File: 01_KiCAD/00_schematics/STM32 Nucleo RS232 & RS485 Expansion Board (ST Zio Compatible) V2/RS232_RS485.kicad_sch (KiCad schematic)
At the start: 28 parts, among them J1 HD-A(Y), J2 HD-B(Z), J3 TERM (A/B), J4 TERM (Y/Z), J5 1190299, J6 CONN D-SUB PLUG 9POS TH, J7 TCVR PWR, U3 THVD4431

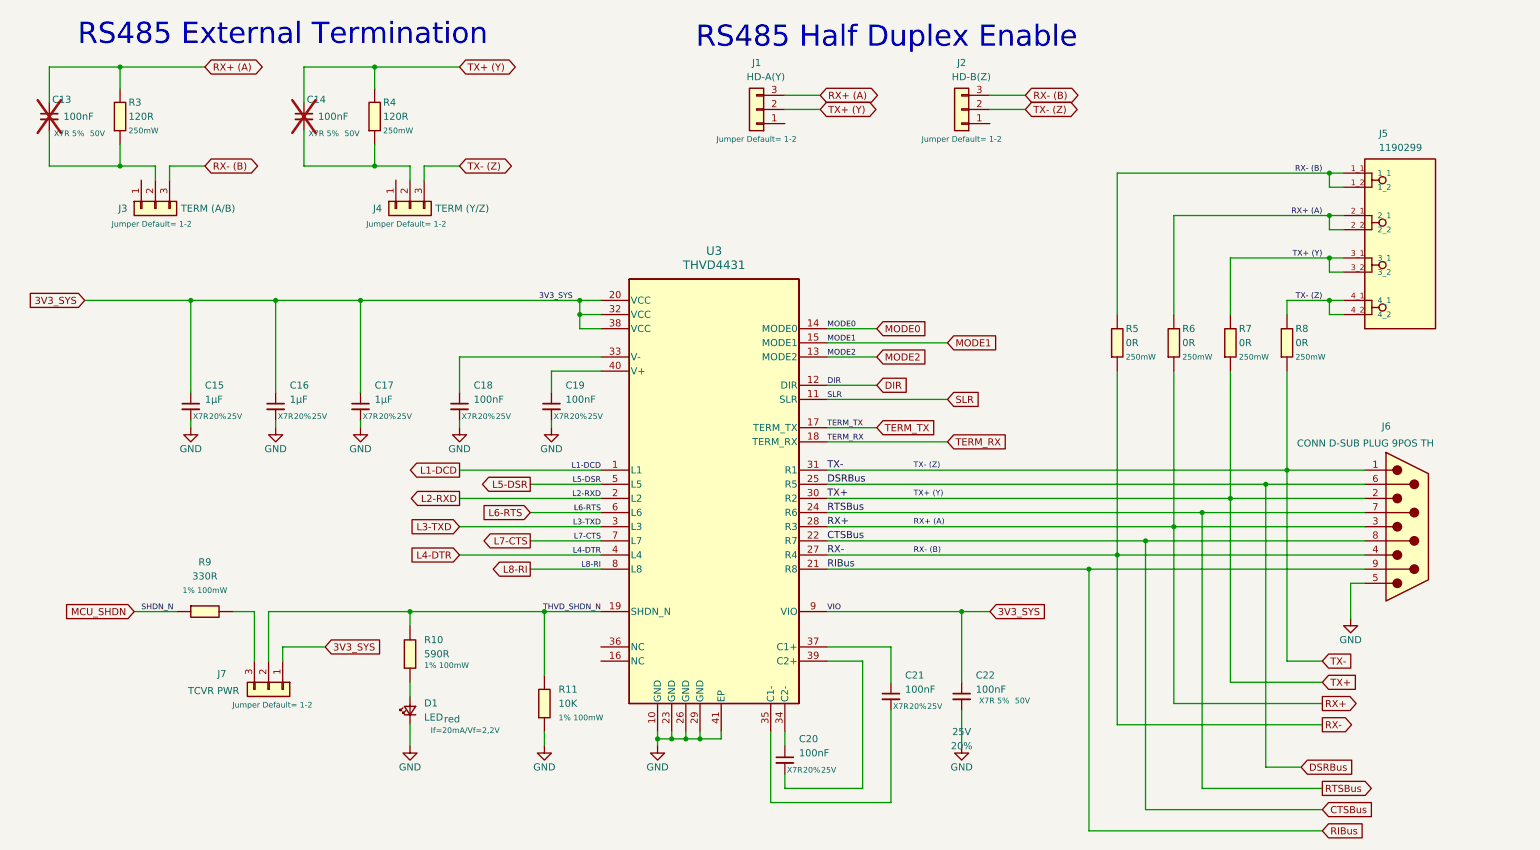
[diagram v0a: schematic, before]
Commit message: Final revision checkup
After BOM-update and corrected some footprints and package sizes for resistors and capacitors, updated the PCB to "HW REV A0.2" as final PCB layout. Need to run DRC check before final approval.
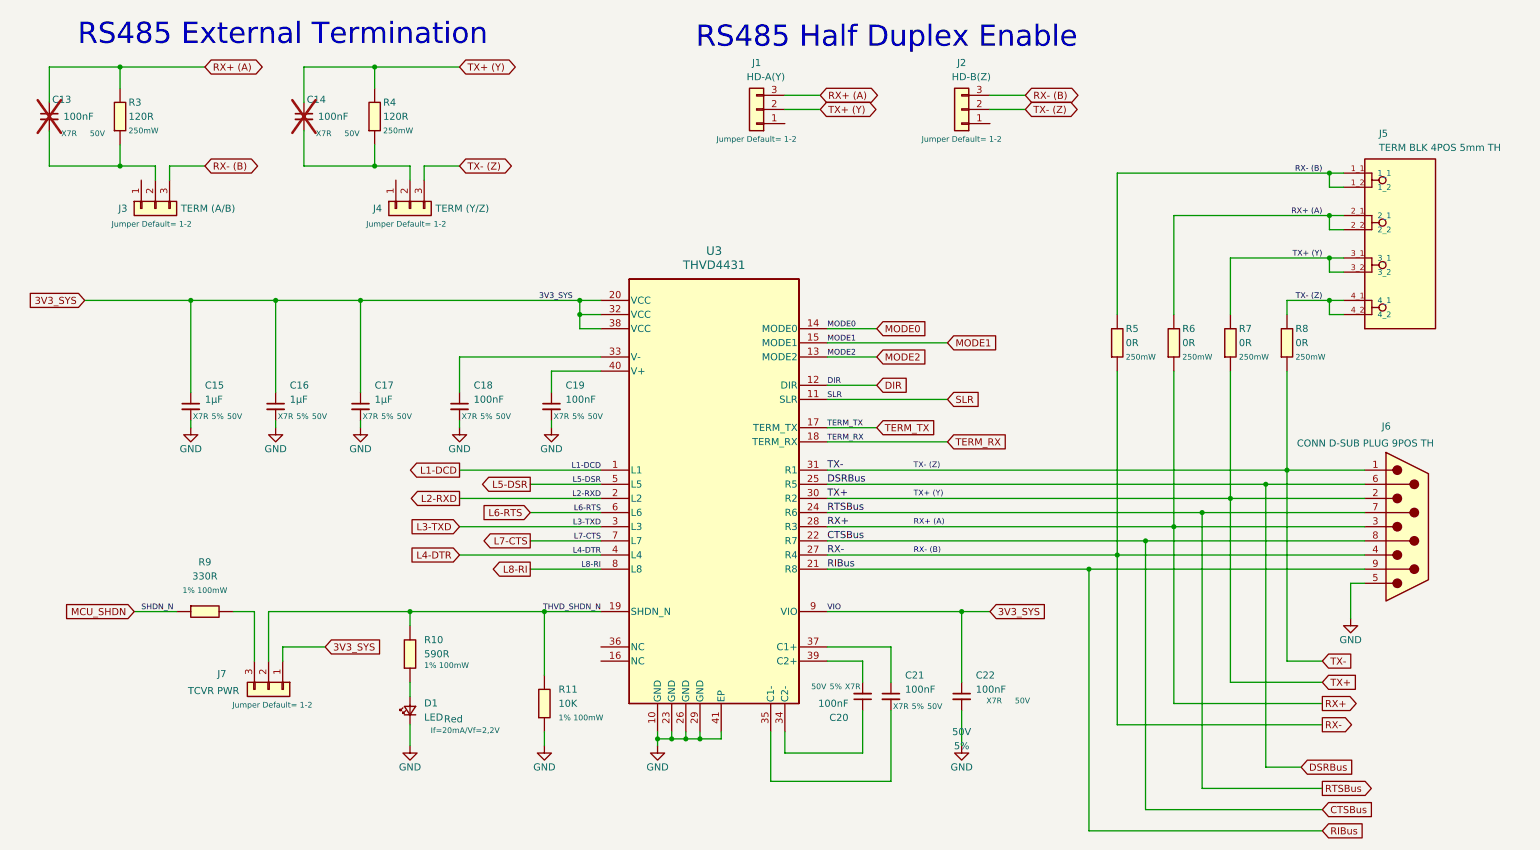
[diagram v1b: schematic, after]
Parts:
- C13, C14: footprint PCM_SparkFun-Capacitor:C_0603_1608Metric -> Capacitor_SMD:C_0805_2012Metric; Dielectric X7R 5% -> X7R; LCSC C91183 -> C2167095; MPN CC0603JRX7R9BB104 -> C0805C104J5RACTU; Manufacturer YAGEO -> KEMET; Mouser PN (none) -> 80-C0805C104J5R; Package 0603 -> 0805; Tolerance 20% -> 5%; Voltage 25V -> 50V
- C15, C16, C17: Mouser PN (none) -> 581-12065C105JAT2A; Tolerance 20% -> 5%; Voltage 25V -> 50V
- C18, C19, C20, C21: Mouser PN (none) -> 80-C0805C104J5R; Tolerance 20% -> 5%; Voltage 25V -> 50V
- C22: Dielectric X7R 5% -> X7R; LCSC C91183 -> C2167095; MPN CC0603JRX7R9BB104 -> C0805C104J5RACTU; Manufacturer YAGEO -> KEMET; Mouser PN (none) -> 80-C0805C104J5R; Package 0603 -> 0805; Tolerance 20% -> 5%; Voltage 25V -> 50V
- D1: Color red -> Red; LCSC C7286681 -> C6639626; MPN HSMZ-C190 -> IN-S63ATR; Manufacturer Broadcom -> Inolux; Mouser PN (none) -> 743-S63ATR; Voltage (none) -> 2,2V
- J1: LCSC C6631883 -> C5714562; MPN HTSW-103-07-F-S -> HTSW-103-07-G-S; Mouser PN (none) -> 200-HTSW10307GS
- J2, J3, J4, J7: LCSC C6631883 -> C5714562; Mouser PN (none) -> 200-HTSW10307GS
- J5: value 1190299 -> TERM BLK 4POS 5mm TH; Mouser PN (none) -> 651-1190299; Package None -> Through Hole,P=5mm
- J6: Mouser PN (none) -> 571-2301843-2
- R10: LCSC C22548 -> C227973; MPN RC0603FR-071KL -> AC0603FR-07590RL; Mouser PN (none) -> 603-AC0603FR-07590RL
- R11: LCSC C98220 -> C20142011; MPN RC0603FR-0710KL -> AC0603FR-7W10KL; Mouser PN (none) -> 603-AC0603FR-7W10KL
- R3, R4: LCSC C253507 -> C5552306; MPN PMR03EZPJ000 -> AC0603FR-7W120RL; Manufacturer ROHM -> YAGEO; Mouser PN (none) -> 603-AC0603FR-7W120RL
- R5, R6, R7, R8: footprint PCM_fab:R_0603 -> PCM_SparkFun-Resistor:R_0805_2012Metric; LCSC C253507 -> C844811; MPN PMR03EZPJ000 -> CRCW08050000Z0EAHP; Manufacturer ROHM -> VISHAY; Mouser PN (none) -> 71-CRCW08050000Z0EAH
- R9: LCSC C105881 -> C513549; MPN RC0603FR-07330RL -> AC0603FR-7W330RL; Mouser PN (none) -> 603-AC0603FR-7W330RL
- U3: Mouser PN (none) -> 595-THVD4431RHAR
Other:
- moved on the sheet: C20

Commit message: Changed to HR_REVA0.3
Updates design to PCB HW-REVA0.3 with the folowing changes:

CL_HW_2026_0001
Replaced text on silkscreen D3=>RX and D4=>TX.

CL_HW_2026_0002
Changed MCU_SHDN pin for THVD4431 from CN9-30 to CN9-11 to make it also Arduino compatible
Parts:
- C13, C14: DNP (none) -> DNP
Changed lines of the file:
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@@
 			)
 		)
-		(property "DNP" ""
+		(property "DNP" "DNP"
 			(at 74.93 33.02 0)
 			(effects
@@
 			)
 		)
-		(property "DNP" ""
+		(property "DNP" "DNP"
 			(at 29.21 33.02 0)
 			(effects
@@
 			(at 29.21 33.02 0)
 			(effects
+				(font
+					(size 1.27 1.27)
+				)
+				(hide yes)
+			)
+		)
+		(property "Farnell PN" ""
+			(at 29.21 33.02 0)
+			(effects
+				(font
+					(size 1.27 1.27)
+				)
+				(hide yes)
+			)
+		)
+		(property "DigiKey PN" ""
+			(at 29.21 33.02 0)
+			(effects
+				(font
+					(size 1.27 1.27)
+				)
+				(hide yes)
+			)
+		)
+		(property "Series" ""
+			(at 29.21 33.02 0)
+			(effects

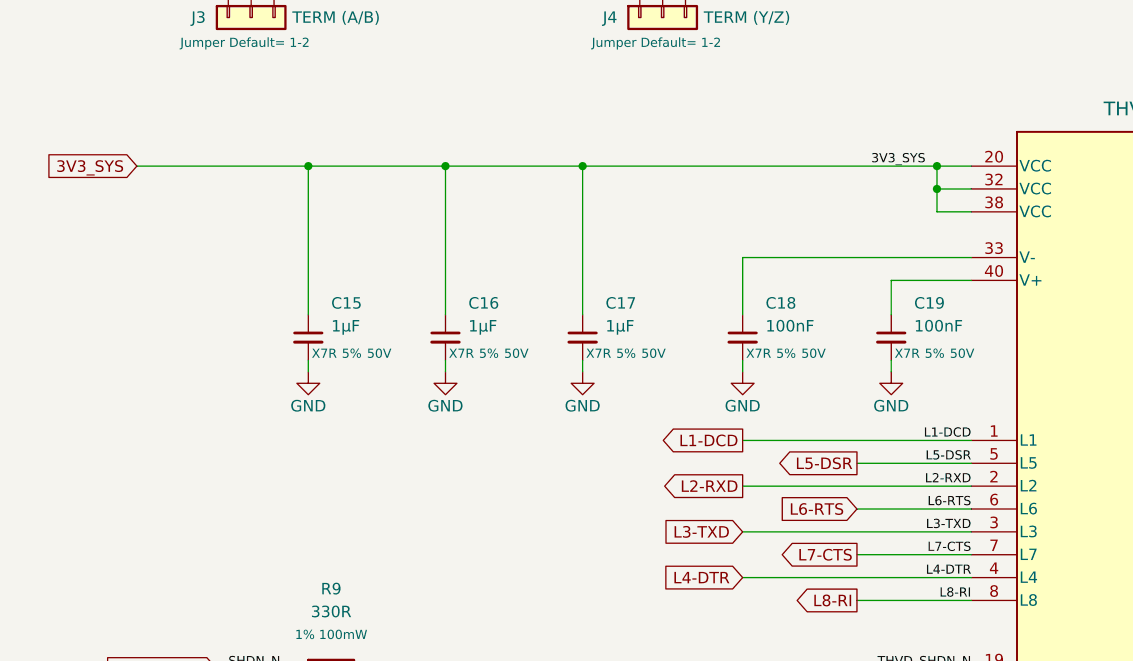
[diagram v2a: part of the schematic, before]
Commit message: Finilizing HW_REVA0.3
See also CL_HW_2026_0003
Added pull-up resistor to L2 on TI advise
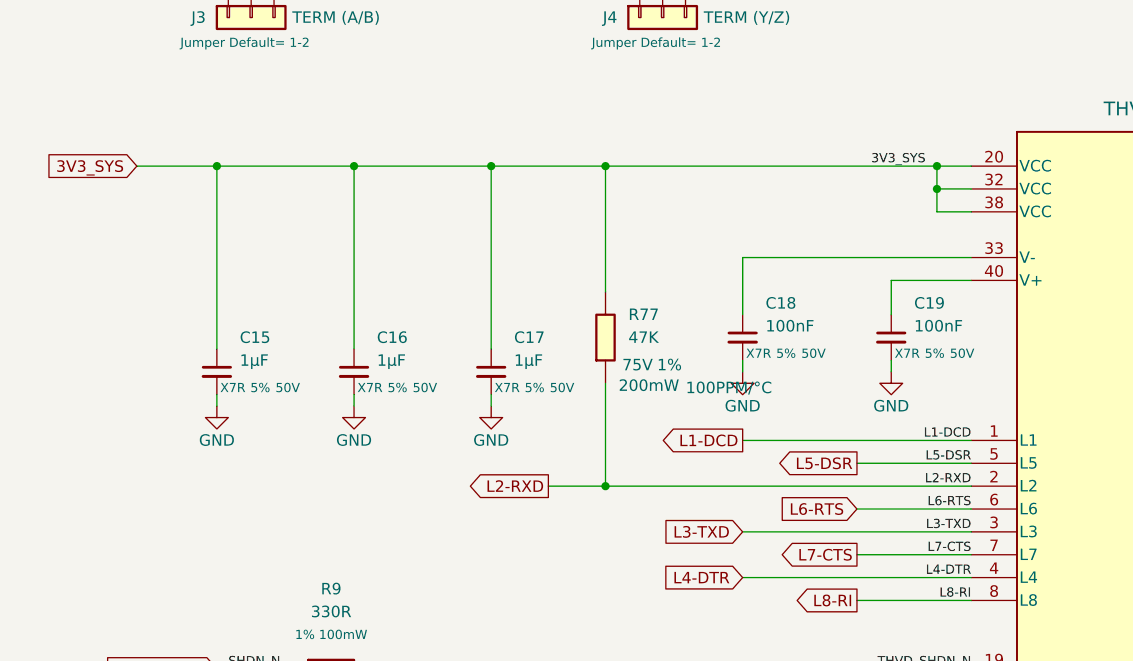
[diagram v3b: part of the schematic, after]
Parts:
- added R77: 47K, PCM_fab:R_0603, symbol PCM_fab:R_0603
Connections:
- net 3V3_SYS: now also R77.1
- net L2-RXD: now also R77.2
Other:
- moved on the sheet: C15, C16, C17
